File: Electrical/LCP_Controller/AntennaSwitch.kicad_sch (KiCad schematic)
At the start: 6 parts, among them J33 Conn_Coaxial, U11 AS179-92LF

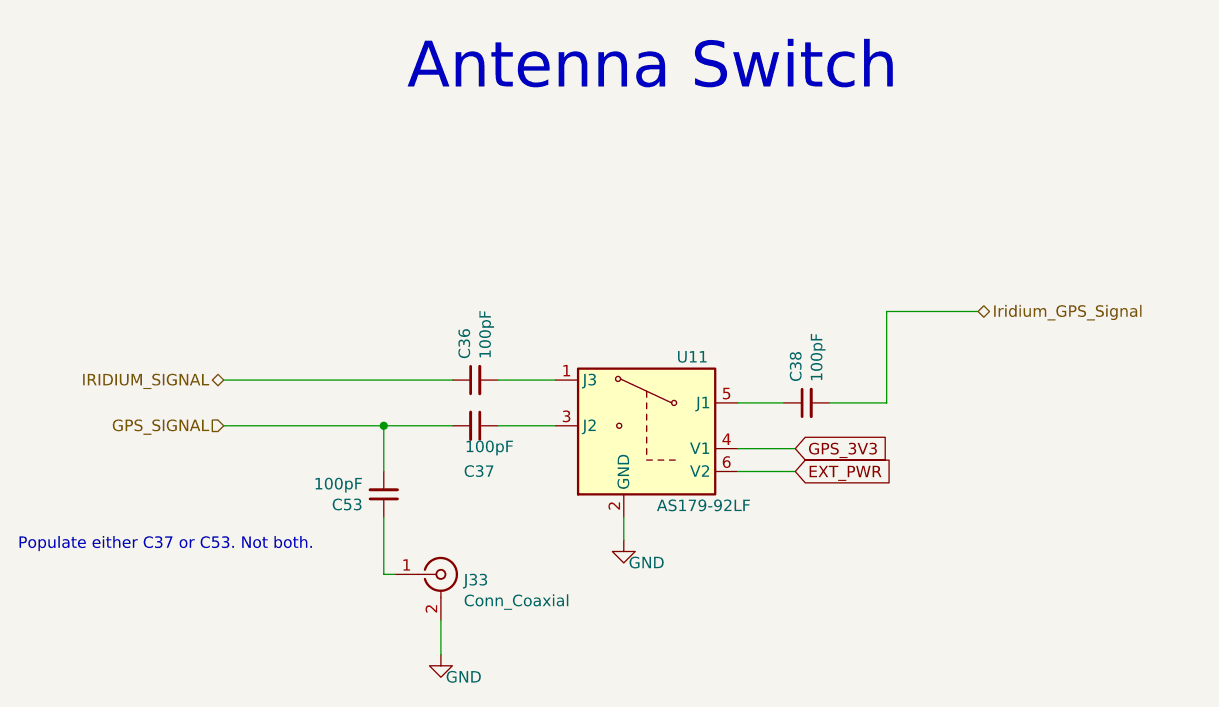
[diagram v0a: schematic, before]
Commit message: Hardware Revision : v0.3
1. modified schematic design, removed unnecessary test points.
2. pcb layout 2x8 Inches allowance dimension, layout is in progress
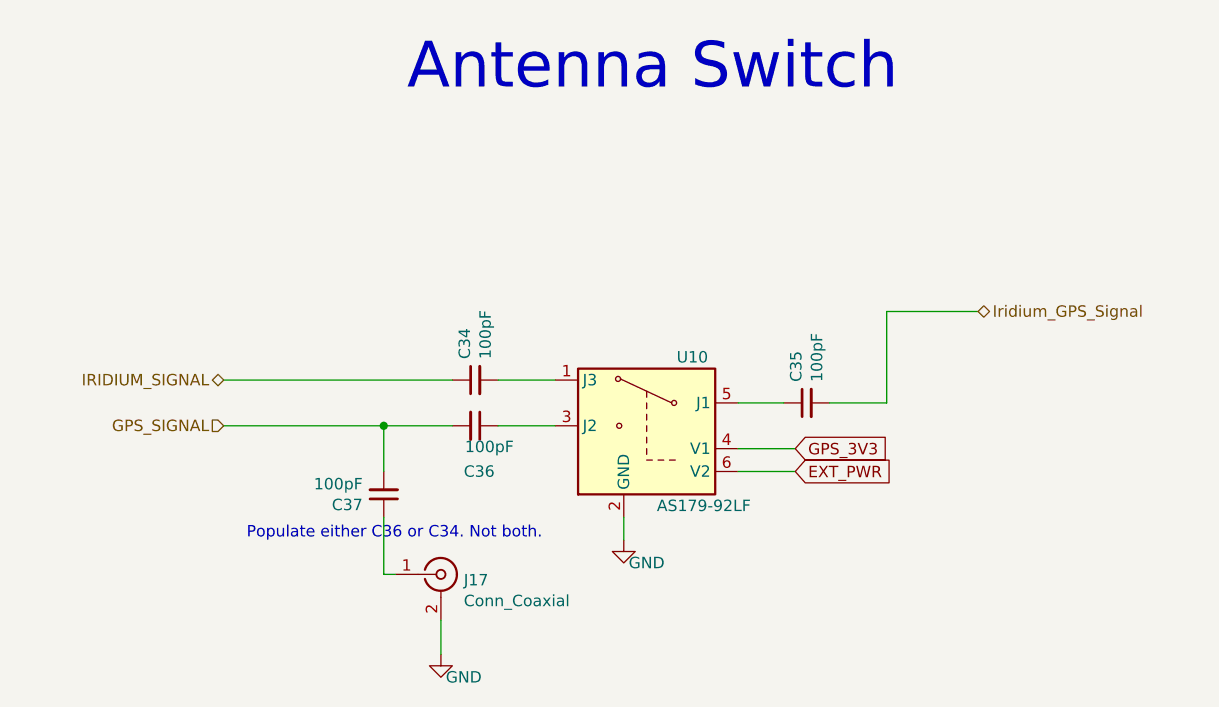
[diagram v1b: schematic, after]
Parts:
- renumbered C36 to C34, C38 to C35, C37 to C36, C53 to C37, J33 to J17, U11 to U10
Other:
- note added: "Populate either C36 or C34. Not both."
- note removed: "Populate either C37 or C53. Not both."
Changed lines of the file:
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@@
     (effects (font (size 5.08 5.08)) (justify right bottom))
   )
-  (text "Populate either C37 or C53. Not both." (at 82.55 118.11 0)
+  (text "Populate either C36 or C34. Not both." (at 107.95 116.84 0)
     (effects (font (size 1.27 1.27)) (justify left bottom))
   )
@@
   (symbol (lib_id "RF_Switch:AS179-92LF") (at 152.4 104.14 0) (mirror y) (unit 1)
     (in_bom yes) (on_board yes)
-    (property "Reference" "U11" (id 0) (at 157.48 96.52 0))
+    (property "Reference" "U10" (id 0) (at 157.48 96.52 0))
     (property "Value" "AS179-92LF" (id 1) (at 158.75 113.03 0))
     (property "Footprint" "Package_TO_SOT_SMD:SOT-363_SC-70-6" (id 2) (at 149.86 104.14 0)
@@
   (symbol (lib_id "Device:C_Small") (at 133.35 99.06 90) (unit 1)
     (in_bom yes) (on_board yes)
-    (property "Reference" "C36" (id 0) (at 132.1816 96.7232 0)
+    (property "Reference" "C34" (id 0) (at 132.1816 96.7232 0)
       (effects (font (size 1.27 1.27)) (justify left))
     )
@@
   (symbol (lib_id "Device:C_Small") (at 133.35 104.14 270) (unit 1)
     (in_bom yes) (on_board yes)
-    (property "Reference" "C37" (id 0) (at 132.08 109.22 90)
+    (property "Reference" "C36" (id 0) (at 132.08 109.22 90)
       (effects (font (size 1.27 1.27)) (justify left))
     )
@@
   (symbol (lib_id "Device:C_Small") (at 170.18 101.6 90) (unit 1)
     (in_bom yes) (on_board yes)
-    (property "Reference" "C38" (id 0) (at 169.0116 99.2632 0)
+    (property "Reference" "C35" (id 0) (at 169.0116 99.2632 0)
       (effects (font (size 1.27 1.27)) (justify left))
     )
@@
   (symbol (lib_id "power:GND") (at 149.86 116.84 0) (unit 1)
     (in_bom yes) (on_board yes)
-    (property "Reference" "#PWR062" (id 0) (at 149.86 123.19 0)
+    (property "Reference" "#PWR081" (id 0) (at 149.86 123.19 0)
       (effects (font (size 1.27 1.27)) hide)
     )
@@
   (symbol (lib_id "Device:C_Small") (at 123.19 111.76 180) (unit 1)
     (in_bom yes) (on_board yes)
-    (property "Reference" "C53" (id 0) (at 120.8532 112.9284 0)
+    (property "Reference" "C37" (id 0) (at 120.8532 112.9284 0)
       (effects (font (size 1.27 1.27)) (justify left))
     )
@@
   (symbol (lib_id "Connector:Conn_Coaxial") (at 129.54 120.65 0) (unit 1)
     (in_bom yes) (on_board yes)
-    (property "Reference" "J33" (id 0) (at 132.08 121.285 0)
+    (property "Reference" "J17" (id 0) (at 132.08 121.285 0)
       (effects (font (size 1.27 1.27)) (justify left))
     )
@@
   (symbol (lib_id "power:GND") (at 129.54 129.54 0) (unit 1)
     (in_bom yes) (on_board yes)
-    (property "Reference" "#PWR0128" (id 0) (at 129.54 135.89 0)
+    (property "Reference" "#PWR082" (id 0) (at 129.54 135.89 0)
       (effects (font (size 1.27 1.27)) hide)
     )

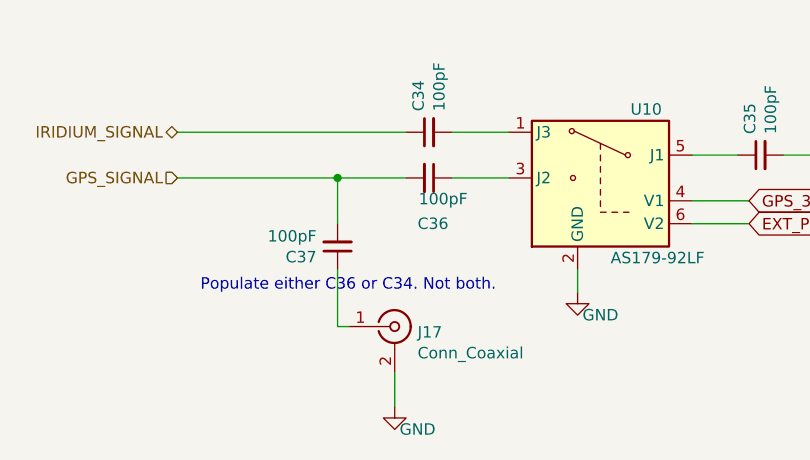
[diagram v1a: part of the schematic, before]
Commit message: Hw Rev : 0.3v
changed buck-coverter LMR50410XDBVR to BD9G102G-LB, added schotty diode.
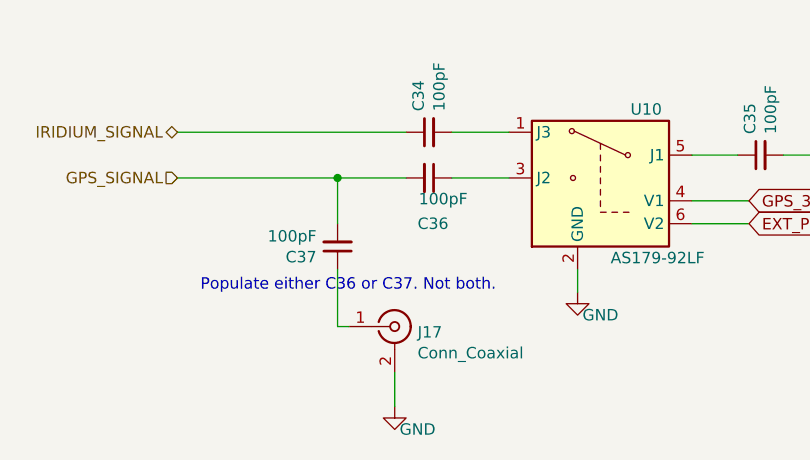
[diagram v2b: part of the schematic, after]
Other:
- note added: "Populate either C36 or C37. Not both."
- note removed: "Populate either C36 or C34. Not both."
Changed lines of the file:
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@@
     (effects (font (size 5.08 5.08)) (justify right bottom))
   )
-  (text "Populate either C36 or C34. Not both." (at 107.95 116.84 0)
+  (text "Populate either C36 or C37. Not both." (at 107.95 116.84 0)
     (effects (font (size 1.27 1.27)) (justify left bottom))
   )

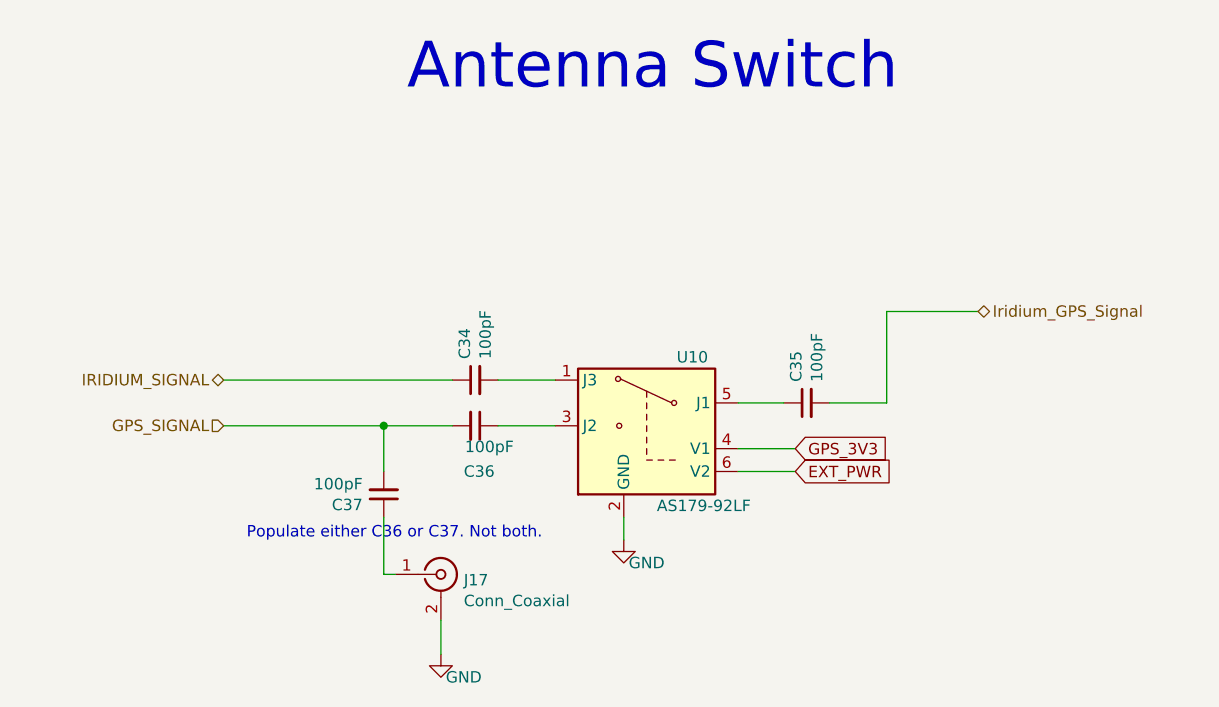
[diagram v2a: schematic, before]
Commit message: Removed RF Switch
Deleted the RF Switch.

GPS Signal is routed to J17 and Iridium to J18.
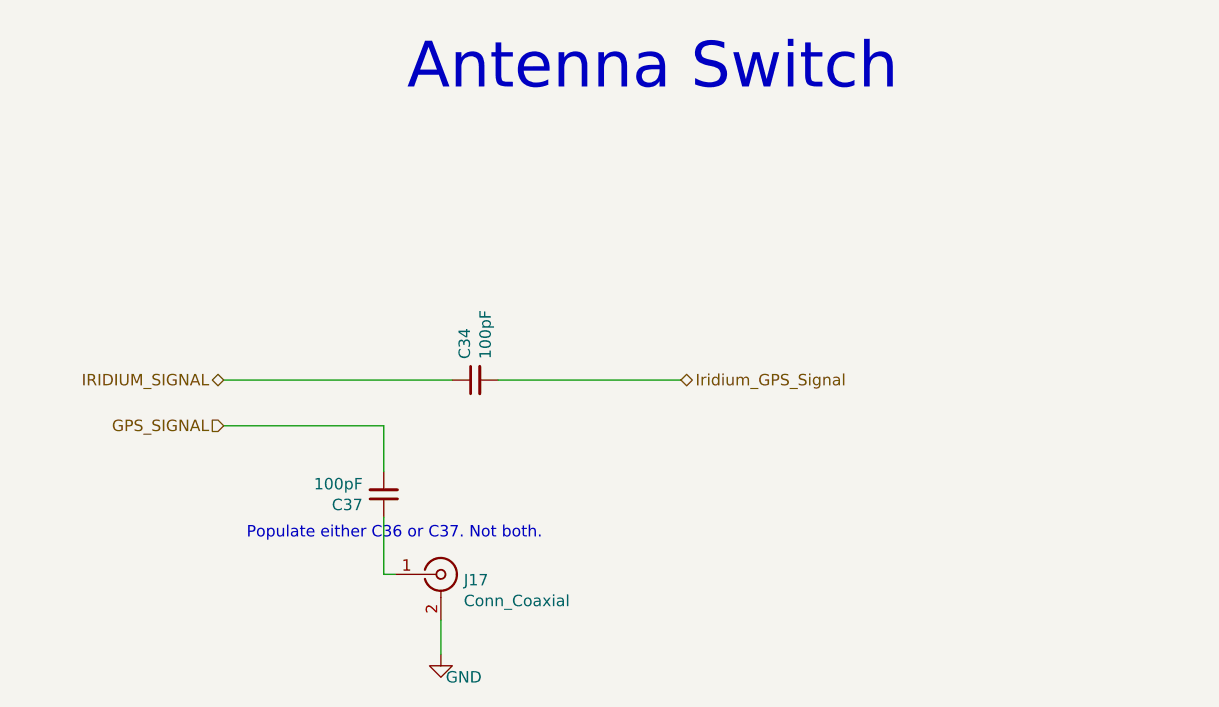
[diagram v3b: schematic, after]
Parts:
- removed C35, C36: 100pF, Capacitor_SMD:C_0805_2012Metric, symbol Device:C_Small
- removed U10: AS179-92LF, Package_TO_SOT_SMD:SOT-363_SC-70-6, symbol RF_Switch:AS179-92LF
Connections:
- net Iridium_GPS_Signal: now also C34.2

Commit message: GPS and Iridium Layout Finalized
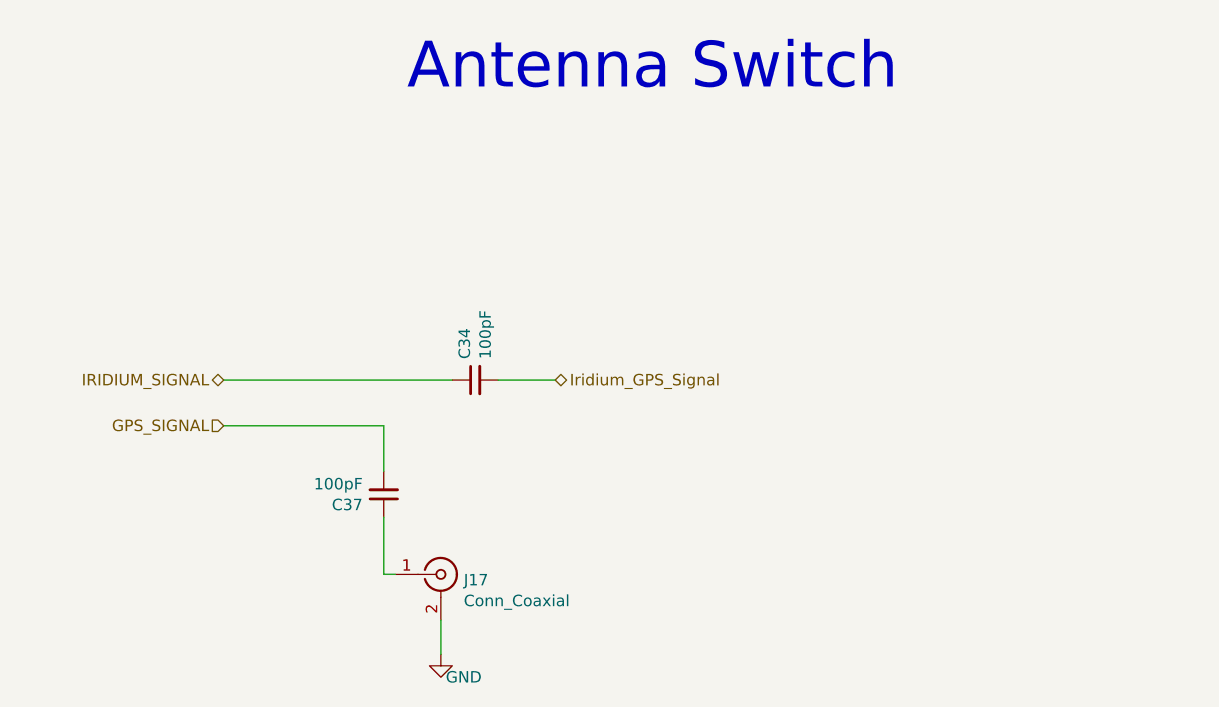
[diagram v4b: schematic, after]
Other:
- note removed: "Populate either C36 or C37. Not both."
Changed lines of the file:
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@@
-    (stroke (width 0) (type default))
-  )
-  (wire (pts (xy 135.89 99.06) (xy 156.21 99.06))
     (stroke (width 0) (type default))
   )
   (wire (pts (xy 123.19 114.3) (xy 123.19 120.65))
+    (stroke (width 0) (type default))
+  )
+  (wire (pts (xy 135.89 99.06) (xy 142.24 99.06))
     (stroke (width 0) (type default))
   )
@@
     (effects (font (size 5.08 5.08)) (justify right bottom))
   )
-  (text "Populate either C36 or C37. Not both." (at 107.95 116.84 0)
-    (effects (font (size 1.27 1.27)) (justify left bottom))
-  )
-  (hierarchical_label "Iridium_GPS_Signal" (shape bidirectional) (at 156.21 99.06 0) (fields_autoplaced)
+  (hierarchical_label "Iridium_GPS_Signal" (shape bidirectional) (at 142.24 99.06 0) (fields_autoplaced)
     (effects (font (size 1.27 1.27)) (justify left))
   )

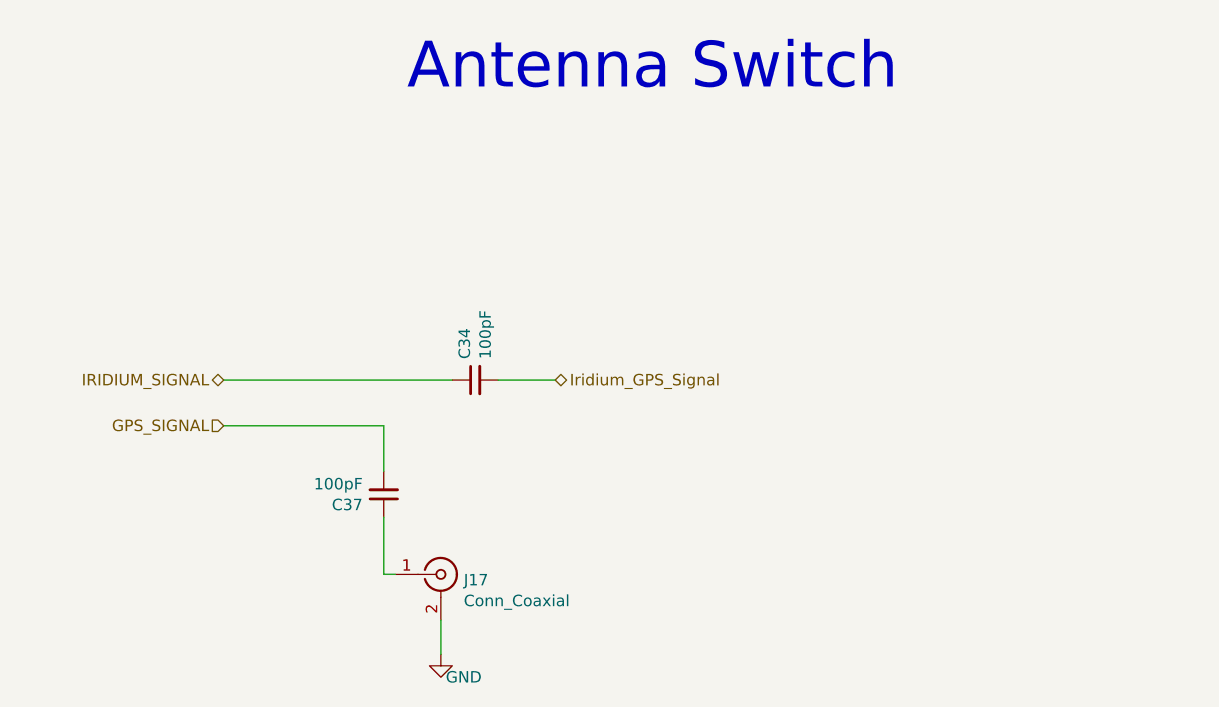
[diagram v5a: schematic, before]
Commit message: New Layout
Changes for this Rev:
- Impedance Matched GPS traces
- Copper Pours
- Vias/Traces changed to bring down costs
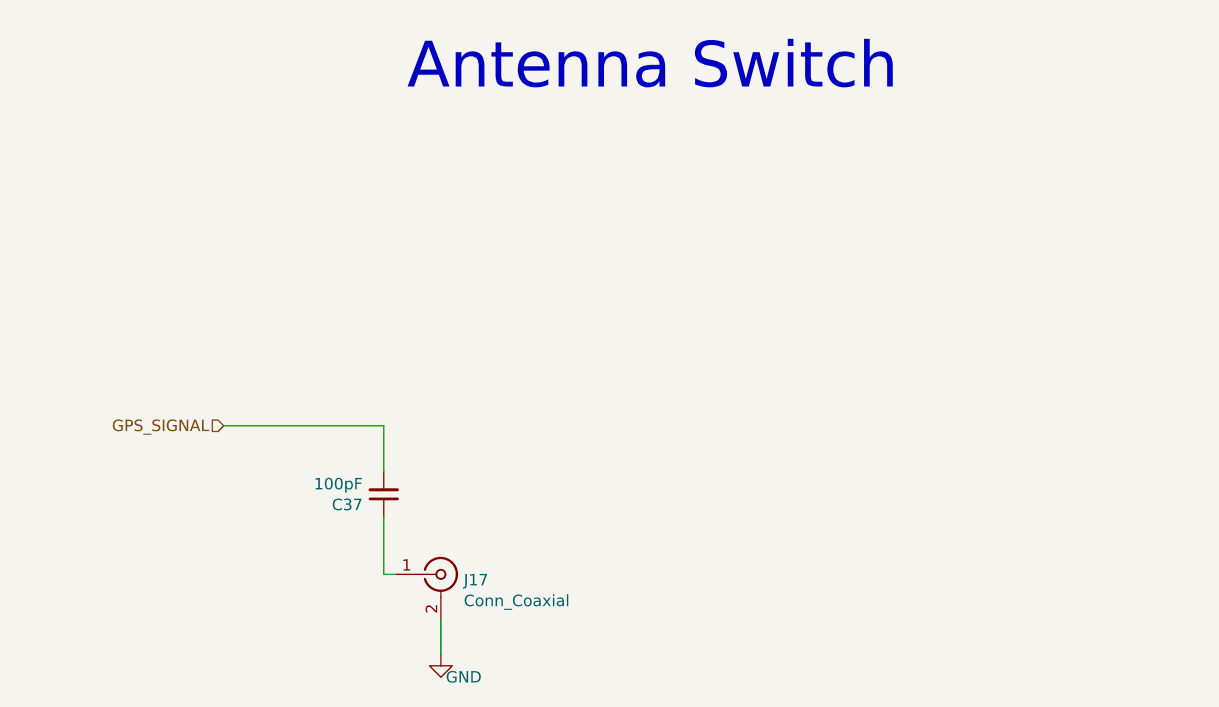
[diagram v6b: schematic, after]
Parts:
- removed C34: 100pF, Capacitor_SMD:C_0805_2012Metric, symbol Device:C_Small
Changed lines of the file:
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@@
-    (stroke (width 0) (type default))
-  )
-  (wire (pts (xy 105.41 99.06) (xy 130.81 99.06))
     (stroke (width 0) (type default))
   )
@@
   )
   (wire (pts (xy 123.19 114.3) (xy 123.19 120.65))
-    (stroke (width 0) (type default))
-  )
-  (wire (pts (xy 135.89 99.06) (xy 142.24 99.06))
     (stroke (width 0) (type default))
   )
@@
     (effects (font (size 5.08 5.08)) (justify right bottom))
   )
-  (hierarchical_label "Iridium_GPS_Signal" (shape bidirectional) (at 142.24 99.06 0) (fields_autoplaced)
-    (effects (font (size 1.27 1.27)) (justify left))
-  )
-  (hierarchical_label "IRIDIUM_SIGNAL" (shape bidirectional) (at 105.41 99.06 180) (fields_autoplaced)
-    (effects (font (size 1.27 1.27)) (justify right))
-  )
   (hierarchical_label "GPS_SIGNAL" (shape input) (at 105.41 104.14 180) (fields_autoplaced)
     (effects (font (size 1.27 1.27)) (justify right))
   )
-  (symbol (lib_id "Device:C_Small") (at 133.35 99.06 90) (unit 1)
-    (in_bom yes) (on_board yes) (dnp no)
-    (property "Reference" "C34" (at 132.1816 96.7232 0)
-      (effects (font (size 1.27 1.27)) (justify left))
-    )
-    (property "Value" "100pF" (at 134.493 96.7232 0)
-      (effects (font (size 1.27 1.27)) (justify left))
-    )
-    (property "Footprint" "Capacitor_SMD:C_0805_2012Metric" (at 133.35 99.06 0)
-      (effects (font (size 1.27 1.27)) hide)
-    )
-    (property "Datasheet" "~" (at 133.35 99.06 0)
-      (effects (font (size 1.27 1.27)) hide)
-    )
-    (property "MPN" "885012207027" (at 133.35 99.06 0)
-      (effects (font (size 1.27 1.27)) hide)
-    )
-    (pin "1")
-    (pin "2")
-    (instances
-      (project "LCP_Controller"
-        (path "/df0f358a-57ab-4ee9-8b36-6ce64ef9d813/00000000-0000-0000-0000-00005ee96a32"
-          (reference "C34") (unit 1)
-        )
-      )
-    )
-  )
   (symbol (lib_id "Device:C_Small") (at 123.19 111.76 180) (unit 1)
